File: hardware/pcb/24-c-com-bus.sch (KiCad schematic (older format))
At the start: 5 parts, among them J401 Conn_01x04, J402 Conn_01x04, U401 MAX3485

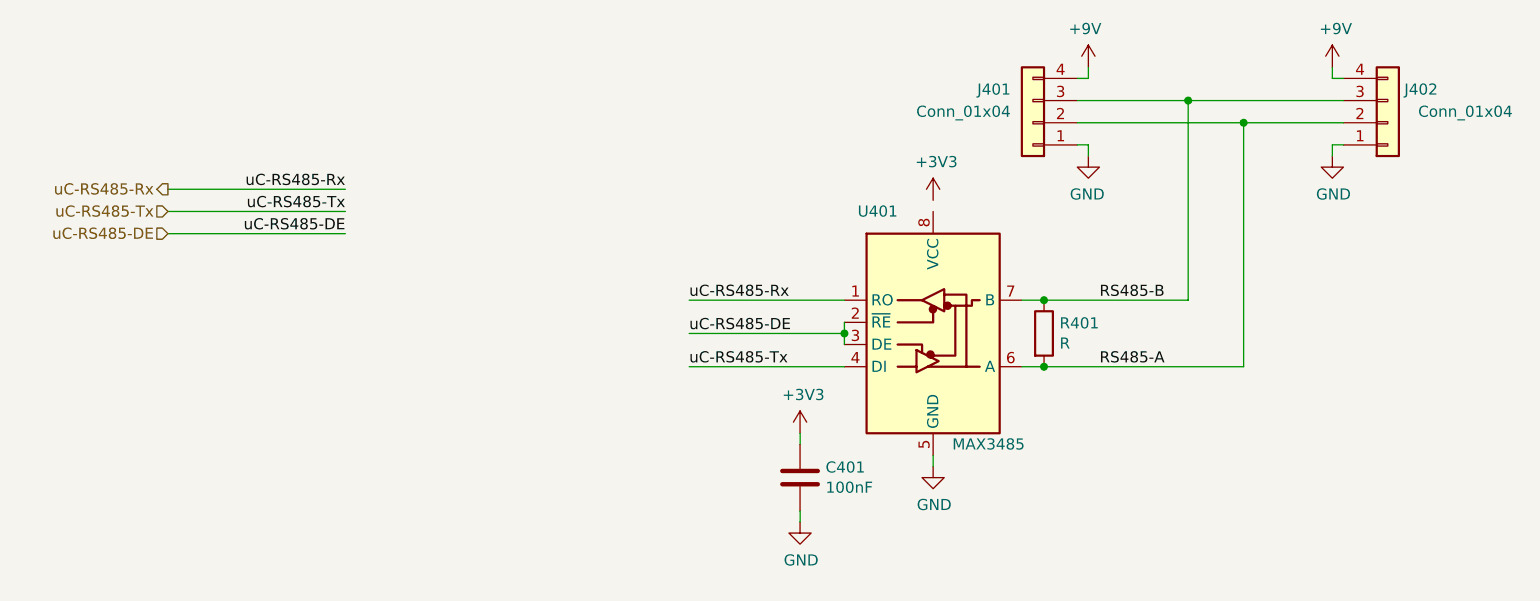
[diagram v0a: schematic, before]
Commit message: Footprints (#2)
* Changed uC

* Updated processor pins and added testpoints

* Small changes

* Updated footprints

* changed crystals

* Created footprints and archived project

* Added motor footprint, made init pcb
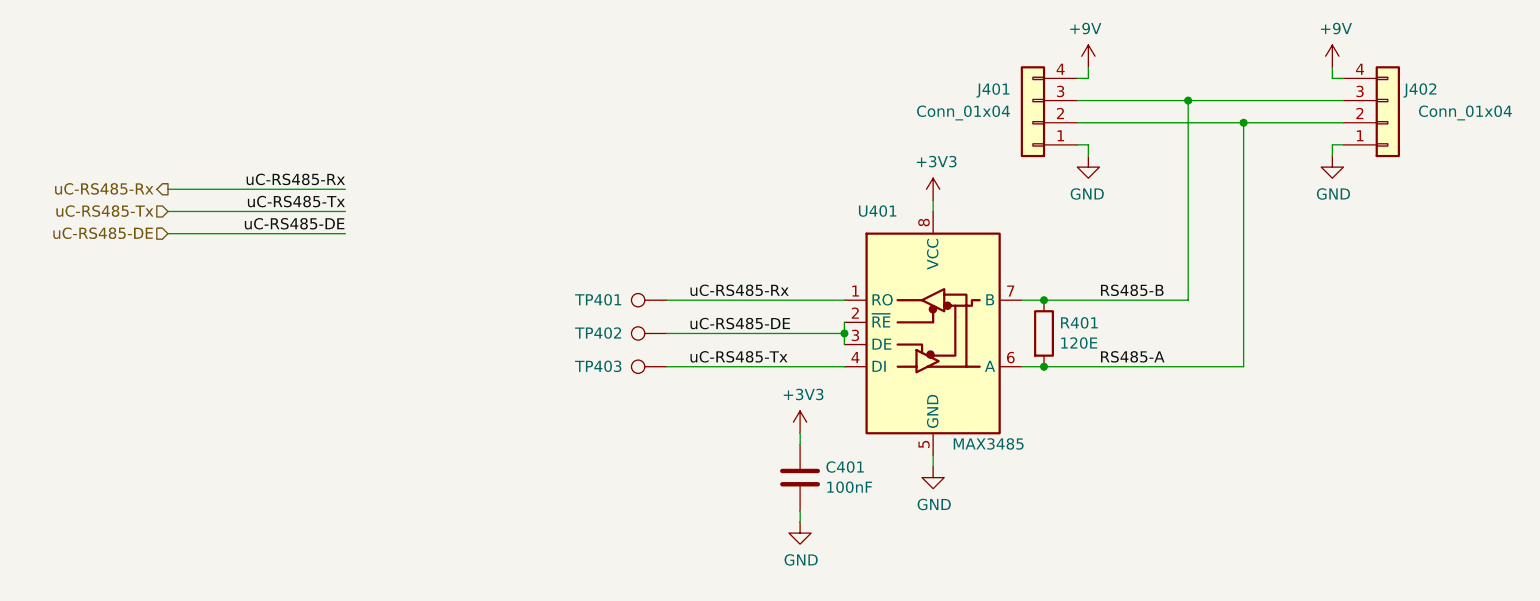
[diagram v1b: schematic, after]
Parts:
- added TP401: uC-RS485-Rx, TestPoint:TestPoint_Pad_D2.0mm, symbol Connector:TestPoint
- added TP402: uC-RS485-DE, TestPoint:TestPoint_Pad_D2.0mm, symbol Connector:TestPoint
- added TP403: uC-RS485-Tx, TestPoint:TestPoint_Pad_D2.0mm, symbol Connector:TestPoint
- C401: footprint C0603 -> Capacitor_SMD:C_0603_1608Metric
- J401, J402: footprint (none) -> Connector_PinHeader_2.54mm:PinHeader_1x04_P2.54mm_Horizontal
- R401: value R -> 120E; footprint (none) -> Resistor_SMD:R_0603_1608Metric
- U401: footprint (none) -> Package_SO:SO-8_3.9x4.9mm_P1.27mm
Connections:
- net +3V3: now also U401.8 (VCC)
- net uC-RS485-DE: now also TP402.1
- net uC-RS485-Rx: now also TP401.1
- net uC-RS485-Tx: now also TP403.1
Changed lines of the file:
@@
 F 0 "U401" H 5400 3450 50  0000 C CNN
 F 1 "MAX3485" H 5900 2400 50  0000 C CNN
-F 2 "" H 5650 2250 50  0001 C CNN
+F 2 "Package_SO:SO-8_3.9x4.9mm_P1.27mm" H 5650 2250 50  0001 C CNN
 F 3 "https://datasheets.maximintegrated.com/en/ds/MAX3483-MAX3491.pdf" H 5650 3000 50  0001 C CNN
 	1    5650 2950
 	1    0    0    -1
 $EndComp
-Wire Wire Line
-	4550 2850 5250 2850
-Wire Wire Line
-	4550 3000 5250 3000
-Wire Wire Line
-	4550 3150 5250 3150
 Wire Wire Line
 	5250 3050 5250 3000
@@
 F 0 "J402" H 7850 1900 50  0000 C CNN
 F 1 "Conn_01x04" H 8050 2000 50  0000 C CNN
-F 2 "" H 7700 2050 50  0001 C CNN
+F 2 "Connector_PinHeader_2.54mm:PinHeader_1x04_P2.54mm_Horizontal" H 7700 2050 50  0001 C CNN
 F 3 "~" H 7700 2050 50  0001 C CNN
 	1    7700 2050
@@
 AR Path="/5FD135B5/5FD2E221" Ref="R401"  Part="1"
 F 0 "R401" H 6220 3046 50  0000 L CNN
-F 1 "R" H 6220 2955 50  0000 L CNN
-F 2 "" V 6080 3000 50  0001 C CNN
+F 1 "120E" H 6220 2955 50  0000 L CNN
+F 2 "Resistor_SMD:R_0603_1608Metric" V 6080 3000 50  0001 C CNN
 F 3 "~" H 6150 3000 50  0001 C CNN
 F 4 "-MASTER,-SLAVE" H 6150 3000 50  0001 C CNN "Config"
@@
 F 0 "C401" H 5165 3696 50  0000 L CNN
 F 1 "100nF" H 5165 3605 50  0000 L CNN
-F 2 "C0603" H 5088 3500 50  0001 C CNN
+F 2 "Capacitor_SMD:C_0603_1608Metric" H 5088 3500 50  0001 C CNN
 F 3 "~" H 5050 3650 50  0001 C CNN
 F 4 "-MASTER" H 5050 3650 50  0001 C CNN "Config"
@@
 F 0 "J401" H 6200 1900 50  0000 L CNN
 F 1 "Conn_01x04" H 6200 2000 50  0000 L CNN
-F 2 "" H 6100 2050 50  0001 C CNN
+F 2 "Connector_PinHeader_2.54mm:PinHeader_1x04_P2.54mm_Horizontal" H 6100 2050 50  0001 C CNN
 F 3 "~" H 6100 2050 50  0001 C CNN
 	1    6100 2050
@@
 Text Label 3000 2550 2    50   ~ 0
 uC-RS485-DE
+Wire Wire Line
+	5650 2450 5650 2400
+$Comp
+L Connector:TestPoint TP401
+U 1 1 5FFCAC49
+P 4450 2850
+F 0 "TP401" V 4450 3050 50  0000 L CNN
+F 1 "uC-RS485-Rx" V 4554 2922 50  0001 C CNN
+F 2 "TestPoint:TestPoint_Pad_D2.0mm" H 4650 2850 50  0001 C CNN
+F 3 "~" H 4650 2850 50  0001 C CNN
+	1    4450 2850
+	0    -1   -1   0
+$EndComp
+$Comp
+L Connector:TestPoint TP402
+U 1 1 5FFCBD49
+P 4450 3000
+F 0 "TP402" V 4450 3200 50  0000 L CNN
+F 1 "uC-RS485-DE" V 4554 3072 50  0001 C CNN
+F 2 "TestPoint:TestPoint_Pad_D2.0mm" H 4650 3000 50  0001 C CNN
+F 3 "~" H 4650 3000 50  0001 C CNN
+	1    4450 3000
+	0    -1   -1   0
+$EndComp
+$Comp
+L Connector:TestPoint TP403
+U 1 1 5FFCBF72
+P 4450 3150
+F 0 "TP403" V 4450 3350 50  0000 L CNN
+F 1 "uC-RS485-Tx" V 4554 3222 50  0001 C CNN
+F 2 "TestPoint:TestPoint_Pad_D2.0mm" H 4650 3150 50  0001 C CNN
+F 3 "~" H 4650 3150 50  0001 C CNN
+	1    4450 3150
+	0    -1   -1   0
+$EndComp
+Wire Wire Line
+	4450 2850 5250 2850
+Wire Wire Line
+	4450 3000 5250 3000
+Wire Wire Line
+	4450 3150 5250 3150
 $EndSCHEMATC

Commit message: Created PCB outline and first placement
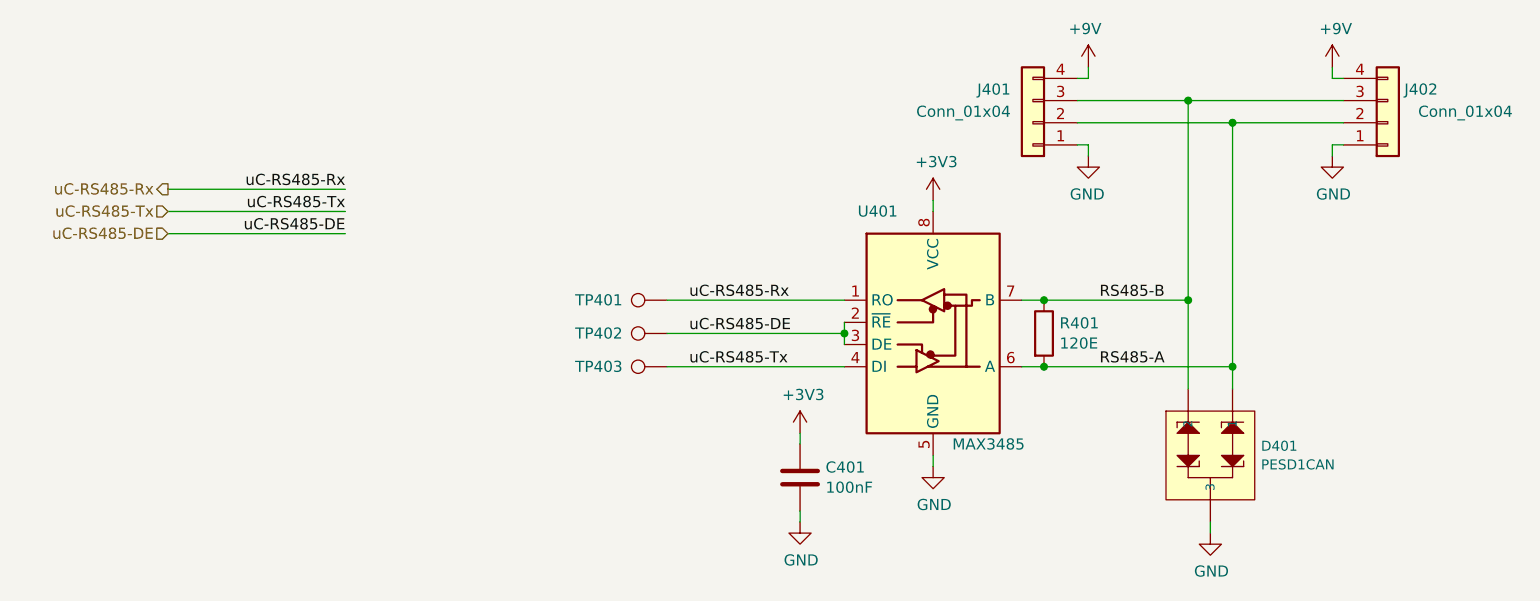
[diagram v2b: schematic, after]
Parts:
- added D401: PESD1CAN, Package_TO_SOT_SMD:SOT-23, symbol SparkFun-DiscreteSemi:PESD1CAN
- J401, J402: footprint Connector_PinHeader_2.54mm:PinHeader_1x04_P2.54mm_Horizontal -> Connector_JST:JST_XH_S4B-XH-A-1_1x04_P2.50mm_Horizontal
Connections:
- net GND: now also D401.3
- net RS485-A: now also D401.1
- net RS485-B: now also D401.2
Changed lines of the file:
@@
 F 0 "J402" H 7850 1900 50  0000 C CNN
 F 1 "Conn_01x04" H 8050 2000 50  0000 C CNN
-F 2 "Connector_PinHeader_2.54mm:PinHeader_1x04_P2.54mm_Horizontal" H 7700 2050 50  0001 C CNN
+F 2 "Connector_JST:JST_XH_S4B-XH-A-1_1x04_P2.50mm_Horizontal" H 7700 2050 50  0001 C CNN
 F 3 "~" H 7700 2050 50  0001 C CNN
 	1    7700 2050
@@
 F 0 "J401" H 6200 1900 50  0000 L CNN
 F 1 "Conn_01x04" H 6200 2000 50  0000 L CNN
-F 2 "Connector_PinHeader_2.54mm:PinHeader_1x04_P2.54mm_Horizontal" H 6100 2050 50  0001 C CNN
+F 2 "Connector_JST:JST_XH_S4B-XH-A-1_1x04_P2.50mm_Horizontal" H 6100 2050 50  0001 C CNN
 F 3 "~" H 6100 2050 50  0001 C CNN
 	1    6100 2050
@@
 	6300 1950 6800 1950
 Wire Wire Line
-	6300 2050 7050 2050
+	6300 2050 7000 2050
 Wire Wire Line
 	6800 2850 6800 1950
@@
 	6800 1950 7500 1950
 Wire Wire Line
-	7050 3150 7050 2050
-Connection ~ 7050 2050
-Wire Wire Line
-	7050 2050 7500 2050
+	7000 3150 7000 2050
+Connection ~ 7000 2050
+Wire Wire Line
+	7000 2050 7500 2050
 Text Label 6400 2850 0    50   ~ 0
 RS485-B
@@
 	6150 3150 6050 3150
 Wire Wire Line
-	6150 3150 7050 3150
+	6150 3150 7000 3150
 Wire Wire Line
 	6150 2850 6800 2850
@@
 Wire Wire Line
 	4450 3150 5250 3150
+$Comp
+L SparkFun-DiscreteSemi:PESD1CAN D401
+U 1 1 5FEA3168
+P 6900 3550
+F 0 "D401" V 6858 3778 45  0000 L CNN
+F 1 "PESD1CAN" V 6942 3778 45  0000 L CNN
+F 2 "Package_TO_SOT_SMD:SOT-23" H 6900 3900 20  0001 C CNN
+F 3 "https://assets.nexperia.com/documents/data-sheet/PESD1CAN.pdf" H 6900 3550 50  0001 C CNN
+	1    6900 3550
+	0    1    1    0
+$EndComp
+Wire Wire Line
+	6800 2850 6800 3250
+Connection ~ 6800 2850
+Wire Wire Line
+	7000 3150 7000 3250
+Connection ~ 7000 3150
+$Comp
+L power:GND #PWR?
+U 1 1 5FEA7BEF
+P 6900 3900
+AR Path="/5FEA7BEF" Ref="#PWR?"  Part="1"
+AR Path="/5FD135B5/5FEA7BEF" Ref="#PWR0409"  Part="1"
+F 0 "#PWR0409" H 6900 3650 50  0001 C CNN
+F 1 "GND" H 6905 3727 50  0000 C CNN
+F 2 "" H 6900 3900 50  0001 C CNN
+F 3 "" H 6900 3900 50  0001 C CNN
+	1    6900 3900
+	1    0    0    -1
+$EndComp
+Wire Wire Line
+	6900 3900 6900 3850
 $EndSCHEMATC
